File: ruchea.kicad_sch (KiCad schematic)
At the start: 13 parts, among them J10 Conn_01x04, J11 Conn_01x04, J12 Conn_01x04, J2 Conn_01x04, J3 Conn_01x03, J4 Conn_01x04, J5 Conn_01x04, J6 Conn_01x02, J7 Conn_01x02, J8 Conn_01x03, J9 Conn_01x03

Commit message: Correction cartouche schéma
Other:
- company: (none) -> Ratamuse
- title: TestboardV2.3a -> Open_beehive_scale_board
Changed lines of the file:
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@@
   (paper "A4")
   (title_block
-    (title "TestboardV2.3a")
-    (date "2021-12-11")
+    (title "Open_beehive_scale_board")
+    (date "2022-05-09")
+    (rev "V0.1")
+    (company "Ratamuse")
   )
   (junction (at 224.79 74.93) (diameter 0) (color 0 0 0 0)

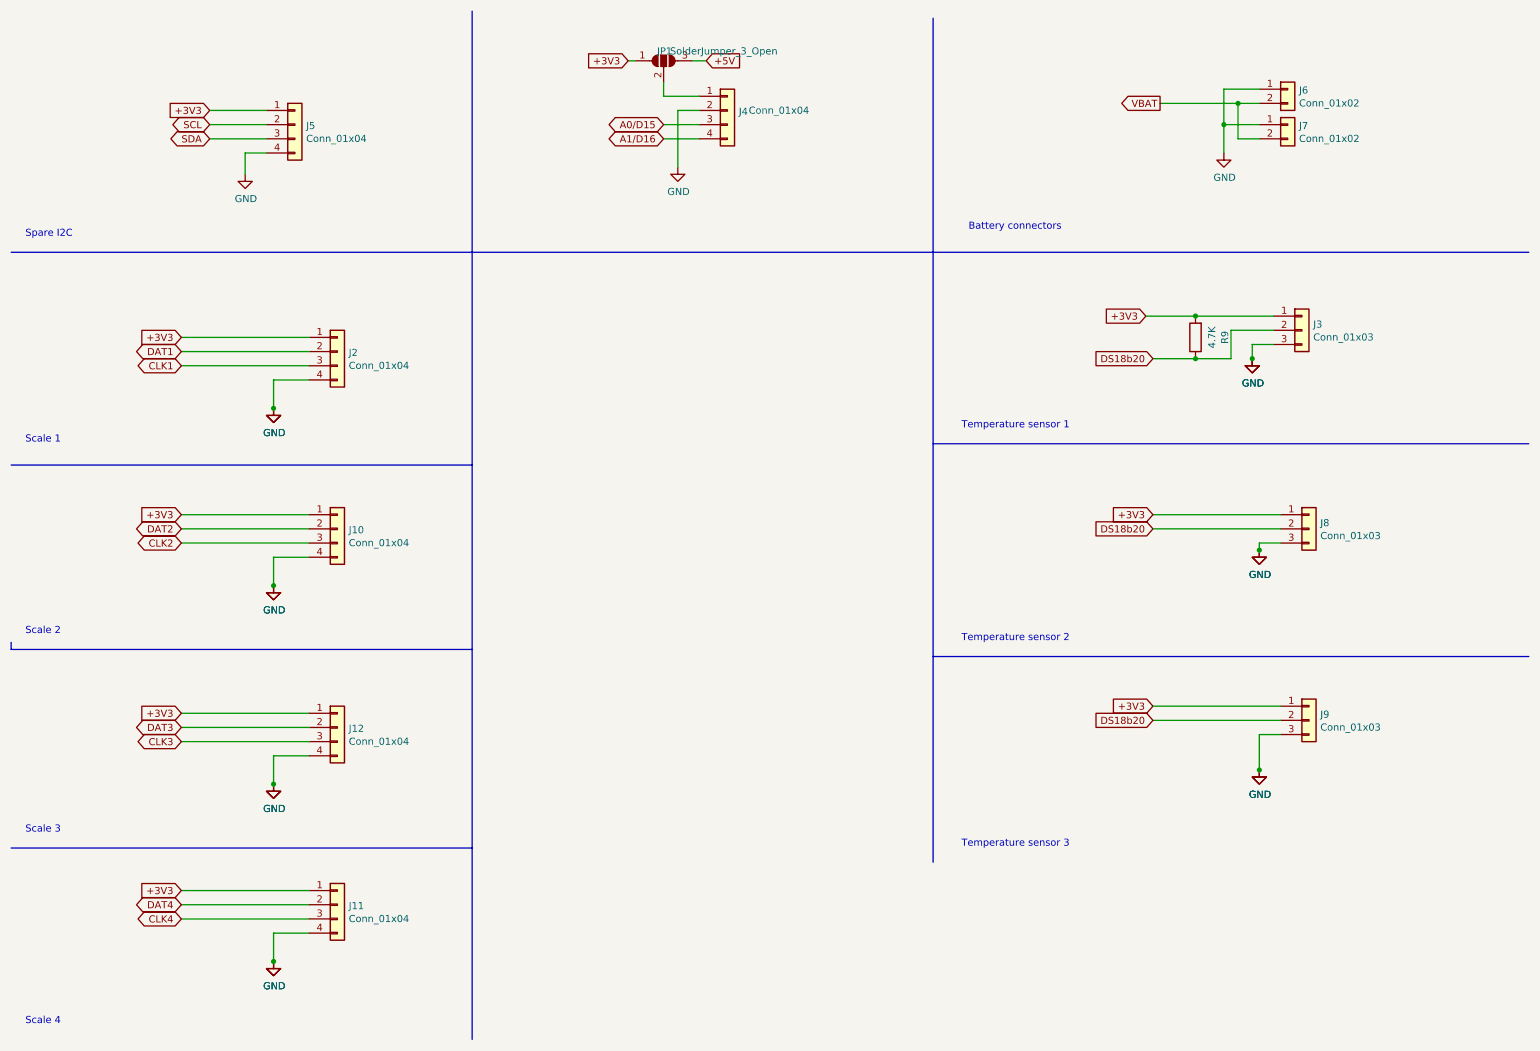
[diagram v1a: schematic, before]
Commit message: add temp sensor
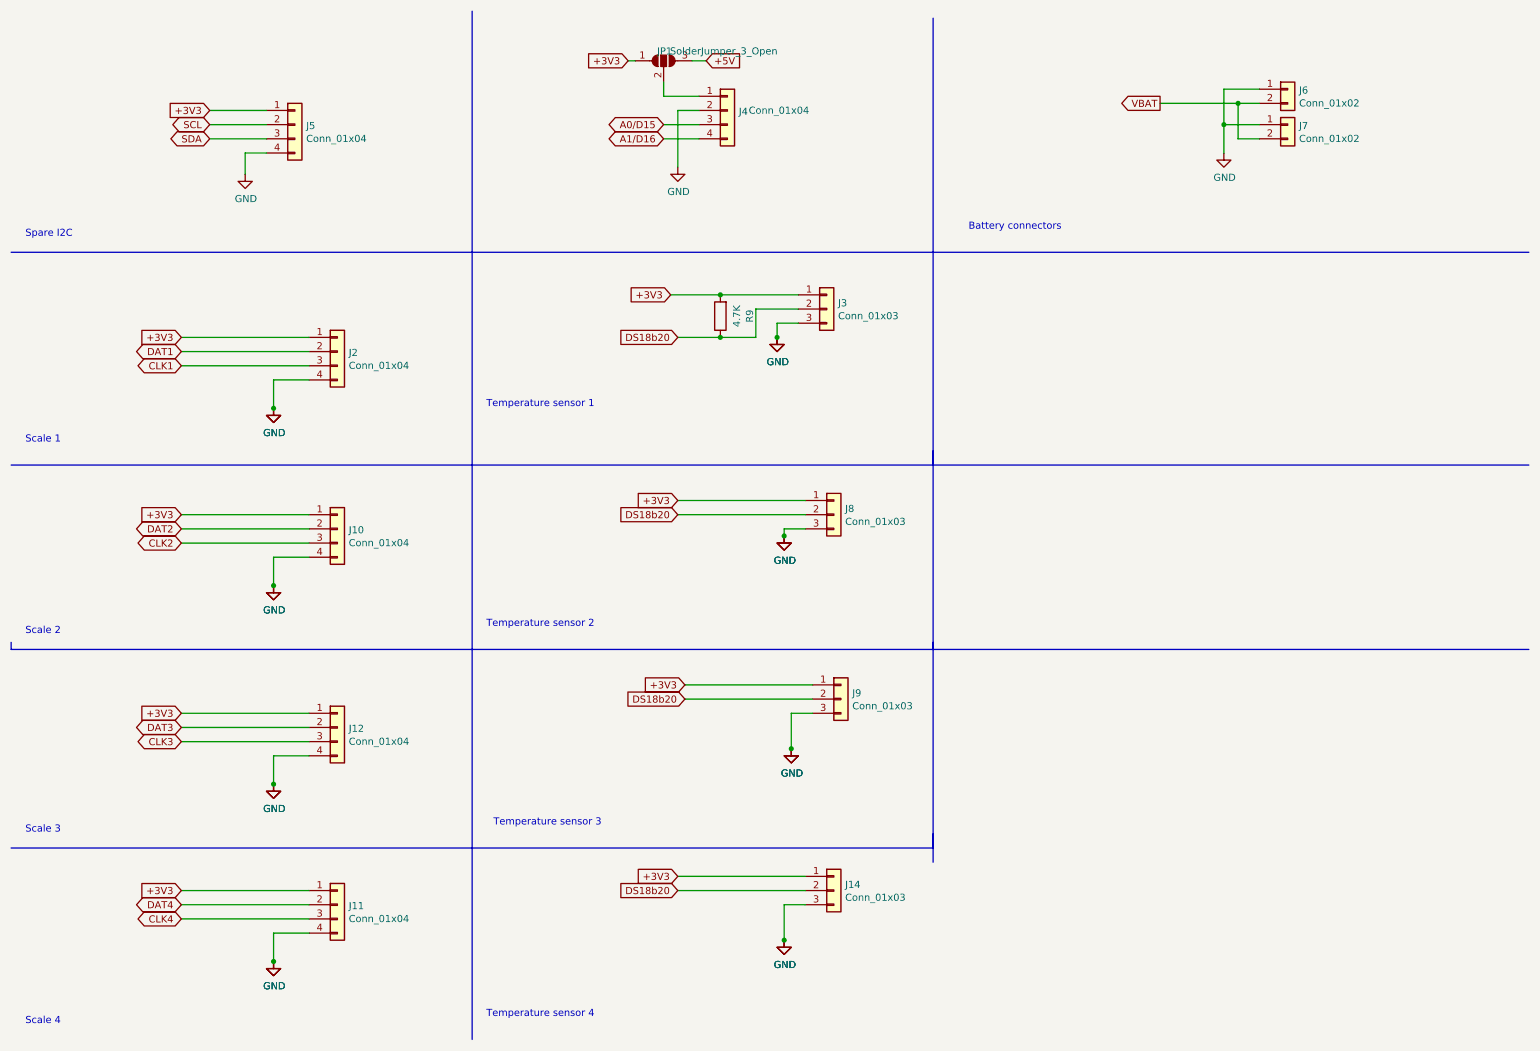
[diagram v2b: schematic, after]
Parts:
- added J14: Conn_01x03, Connector_JST:JST_PH_B3B-PH-K_1x03_P2.00mm_Vertical, symbol Connector_Generic:Conn_01x03
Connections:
- net +3V3: now also J14.1 (Pin_1)
- net DS18b20: now also J14.2 (Pin_2)
- net GND: now also J14.3 (Pin_3)
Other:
- note added: "Temperature sensor 4"
- moved on the sheet: J3, J8, J9, R9
